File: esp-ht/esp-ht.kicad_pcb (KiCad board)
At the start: 2 copper layers, 25.4 x 54.6 mm, 28 parts, among them P1 CONN_01X02, P2 CONN_01X02, SW1 SW_PUSH_SMALL, SW2 SW_PUSH_SMALL, U1 ESP-12E, U2 MCP1700-3.0, U3 SI7021

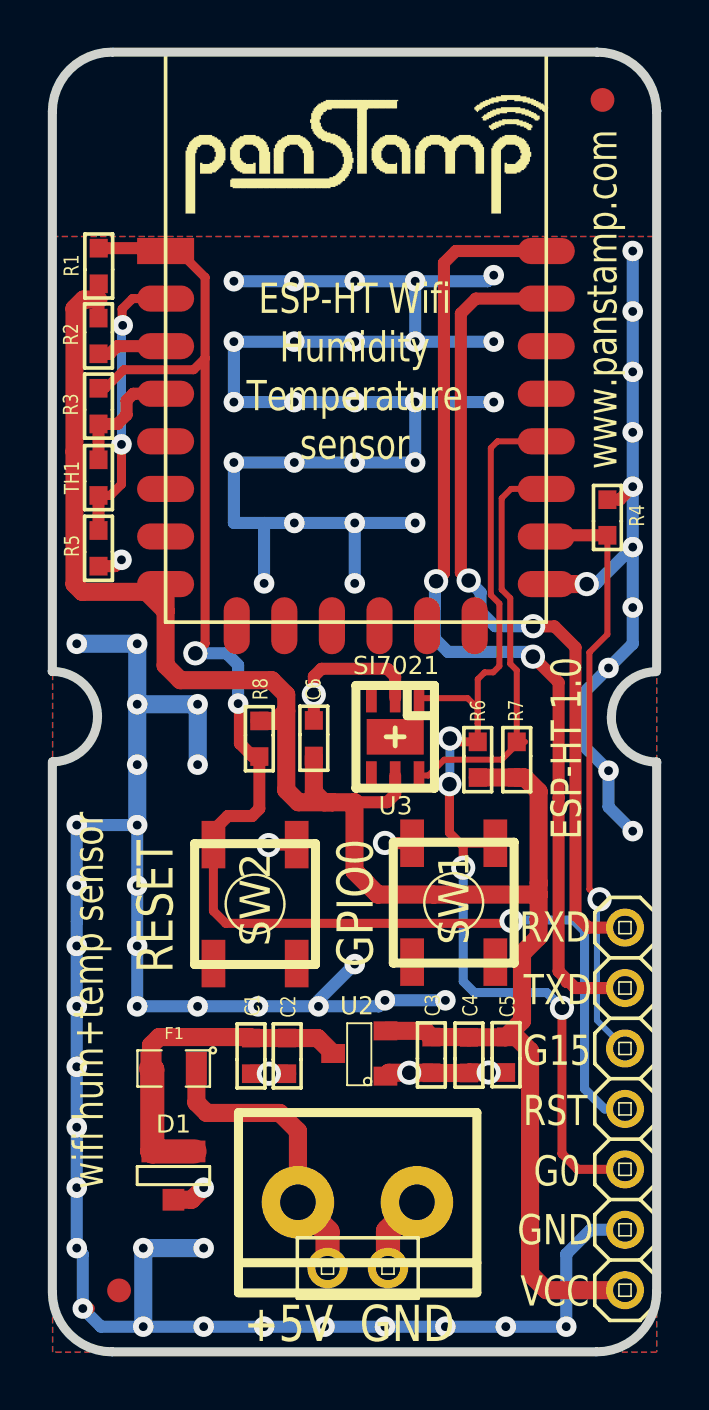
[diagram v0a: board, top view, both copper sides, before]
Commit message: BMP180 pressure sensor added to the circuit
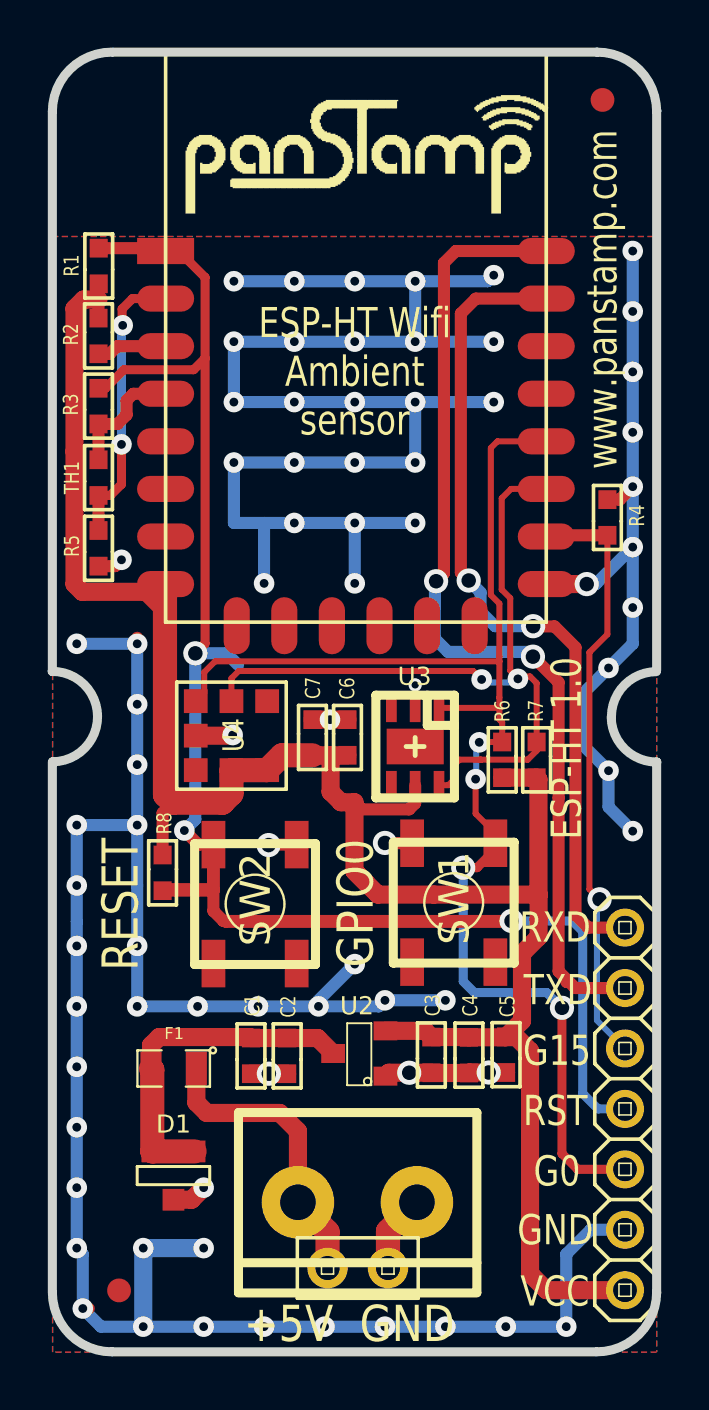
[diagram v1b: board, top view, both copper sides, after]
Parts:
- added C7: 1u, mysmd:SM0603S, F.Cu at (146.8, 73.8)
- added U4: BMP180, mysmd:BMP180, F.Cu at (143.4, 73.7)
- moved R8 6.95 mm to (140.5, 79.5)
- moved C6 1.42 mm to (148.3, 73.8)
- moved R6 1.03 mm to (154.8, 74.7)
- moved U3 0.93 mm to (151.1, 74.2)
- moved R7 0.84 mm to (156.2, 74.7)
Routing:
- net /RESET: track 65.2 -> 88.0 mm
- net /GPIO2: track 17.6 -> 32.2 mm, vias 0 -> 2
- net /GPIO0: track 45.6 -> 57.5 mm
- net GND: track 146.9 -> 139.8 mm, vias 54 -> 53
- net VCC: track 93.5 -> 98.2 mm
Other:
- rule via_min_drill: 0.3683 -> 0.3048
- rule via_min_size: 0.8636 -> 0.5588
- board text added: "ESP-HT Wifi Ambient sensor"
- board text removed: "ESP-HT Wifi Humidity Temperature sensor"
- board text removed: "wifi hum+temp sensor"

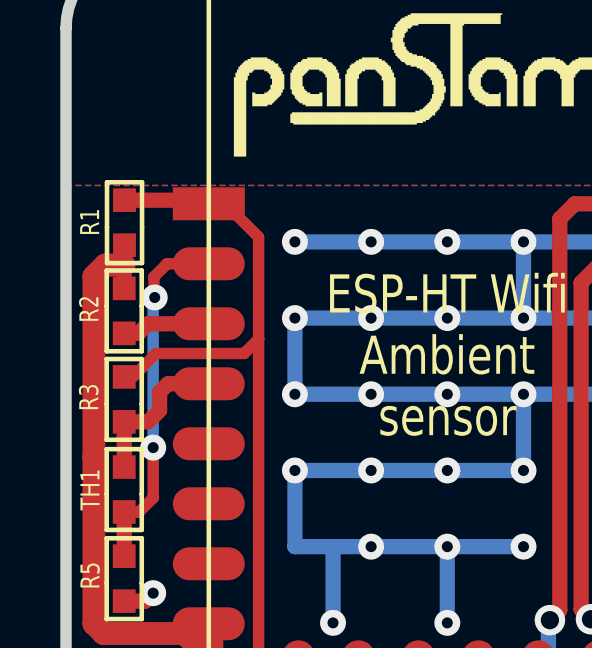
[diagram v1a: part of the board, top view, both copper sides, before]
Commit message: repeated Pull-up resistor (R1)  to RESET removed
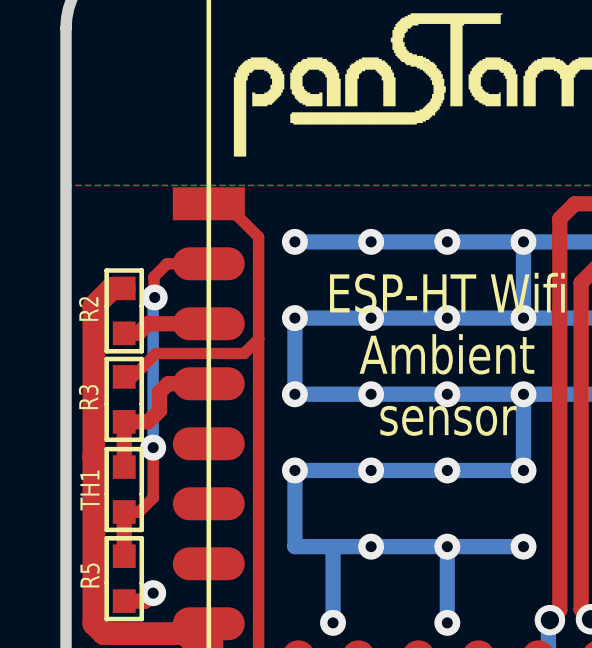
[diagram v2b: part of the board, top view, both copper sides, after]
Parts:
- removed R1: 10k, mysmd:SM0603S
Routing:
- net /RESET: track 88.0 -> 85.4 mm
- net VCC: track 98.2 -> 95.9 mm
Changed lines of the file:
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@@
-(kicad_pcb (version 4) (host pcbnew 0.201511131146+6311~30~ubuntu14.04.1-product)
+(kicad_pcb (version 4) (host pcbnew 0.201512211246+6391~39~ubuntu14.04.1-stable)
   (general
-    (links 62)
+    (links 60)
     (no_connects 0)
-    (area 135.679499 44.789499 161.480501 99.800501)
+    (area 133.447065 41.2496 163.844514 102.9716)
     (thickness 1.6002)
     (drawings 28)
-    (tracks 464)
+    (tracks 460)
     (zones 0)
-    (modules 30)
+    (modules 29)
     (nets 25)
   )
@@
   )
   (setup
-    (last_trace_width 1.016)
+    (last_trace_width 0.762)
     (user_trace_width 0.254)
     (user_trace_width 0.381)
@@
   )
   (module mysmd:SM0603S (layer Front)
-    (at 137.83 53.97 270)
-    (attr smd)
-    (fp_text reference R1 (at -0.02 1.14 270) (layer F.SilkS)
-      (effects (font (size 0.635 0.508) (thickness 0.127)))
-    )
-    (fp_text value 10k (at 0.0762 -0.0254 270) (layer F.SilkS) hide
-      (effects (font (size 0.635 0.508) (thickness 0.127)))
-    )
-    (fp_line (start 0.1524 -0.5842) (end -1.3462 -0.5842) (layer F.SilkS) (width 0.1524))
-    (fp_line (start -1.3462 -0.5842) (end -1.3462 0.5842) (layer F.SilkS) (width 0.1524))
-    (fp_line (start -1.3462 0.5842) (end 0.1524 0.5842) (layer F.SilkS) (width 0.1524))
-    (fp_line (start 0.1524 -0.5842) (end 1.3462 -0.5842) (layer F.SilkS) (width 0.1524))
-    (fp_line (start 1.3462 -0.5842) (end 1.3462 0.5842) (layer F.SilkS) (width 0.1524))
-    (fp_line (start 1.3462 0.5842) (end 0.1524 0.5842) (layer F.SilkS) (width 0.1524))
-    (pad 2 smd rect (at 0.7493 0 270) (size 0.7874 0.762) (layers Front F.Paste F.Mask)
-      (net 11 VCC))
-    (pad 1 smd rect (at -0.7493 0 270) (size 0.7874 0.762) (layers Front F.Paste F.Mask)
-      (net 1 /RESET))
-    (model smd/chip_cms.wrl
-      (at (xyz 0 0 0))
-      (scale (xyz 0.17 0.16 0.16))
-      (rotate (xyz 0 0 0))
-    )
-  )
-  (module mysmd:SM0603S (layer Front)
     (at 137.82 56.91 90)
     (attr smd)
@@
   (segment (start 142.3 54.45) (end 141.19 53.34) (width 0.381) (layer Front) (net 1))
   (segment (start 141.19 53.34) (end 140.64 53.34) (width 0.381) (layer Front) (net 1))
-  (segment (start 137.83 53.2207) (end 140.5207 53.2207) (width 0.508) (layer Front) (net 1))
   (segment (start 140.5207 53.2207) (end 140.64 53.34) (width 0.508) (layer Front) (net 1))
   (via (at 155.18 81.5) (size 1.016) (drill 0.6096) (layers Front Back) (net 1))
@@
   (segment (start 159.21 65.2893) (end 156.6907 65.2893) (width 0.508) (layer Front) (net 10))
   (segment (start 156.6907 65.2893) (end 156.64 65.34) (width 0.508) (layer Front) (net 10))
+  (segment (start 137.82 56.1607) (end 137.4127 56.1607) (width 0.762) (layer Front) (net 11))
+  (segment (start 137.4127 56.1607) (end 136.81 56.7634) (width 0.762) (layer Front) (net 11))
   (segment (start 151.13 75.793) (end 151.13 76.5556) (width 0.508) (layer Front) (net 11))
   (segment (start 148.8796 76.8096) (end 148.58 76.51) (width 0.508) (layer Front) (net 11))
@@
   (segment (start 156.3116 75.5523) (end 156.2354 75.4761) (width 0.762) (layer Front) (net 11))
   (segment (start 136.81 61.77) (end 136.81 67.341) (width 0.762) (layer Front) (net 11))
-  (segment (start 137.19 55.38) (end 136.81 55.76) (width 0.762) (layer Front) (net 11))
-  (segment (start 136.81 55.76) (end 136.81 61.77) (width 0.762) (layer Front) (net 11))
-  (segment (start 137.82 55.38) (end 137.19 55.38) (width 0.762) (layer Front) (net 11))
+  (segment (start 136.81 56.7634) (end 136.81 61.77) (width 0.762) (layer Front) (net 11))
   (segment (start 137.1346 67.6656) (end 139.827 67.6656) (width 0.762) (layer Front) (net 11))
   (segment (start 136.81 67.341) (end 137.1346 67.6656) (width 0.762) (layer Front) (net 11))
@@
   (segment (start 149.07 79.9) (end 148.58 79.41) (width 0.508) (layer Front) (net 11))
   (segment (start 156.32 81.43) (end 156.32 80.39) (width 0.762) (layer Front) (net 11))
-  (segment (start 137.82 56.1607) (end 137.82 55.38) (width 0.508) (layer Front) (net 11))
-  (segment (start 137.82 55.38) (end 137.82 54.7293) (width 0.508) (layer Front) (net 11))
-  (segment (start 137.82 54.7293) (end 137.83 54.7193) (width 0.508) (layer Front) (net 11))
   (segment (start 149.87982 86.1175) (end 151.5468 86.1175) (width 0.762) (layer Front) (net 11))
   (segment (start 151.5468 86.1175) (end 151.81 86.3807) (width 0.762) (layer Front) (net 11))

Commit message: Version changed
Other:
- rule pad_to_mask_clearance: 0.254 -> 0.0762
- board text added: "v.1.0"
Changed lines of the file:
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@@
-(kicad_pcb (version 4) (host pcbnew 0.201512211246+6391~39~ubuntu14.04.1-stable)
+(kicad_pcb (version 4) (host pcbnew 0.201601211448+6504~42~ubuntu14.04.1-product)
   (general
     (links 60)
@@
     (area 133.447065 41.2496 163.844514 102.9716)
     (thickness 1.6002)
-    (drawings 28)
+    (drawings 29)
     (tracks 460)
     (zones 0)
@@
   )
   (setup
-    (last_trace_width 0.762)
+    (last_trace_width 0.1524)
     (user_trace_width 0.254)
     (user_trace_width 0.381)
@@
     (pad_size 1.7 1.7)
     (pad_drill 1.016)
-    (pad_to_mask_clearance 0.254)
+    (pad_to_mask_clearance 0.0762)
+    (solder_mask_min_width 0.1016)
     (aux_axis_origin 0 0)
     (visible_elements FFFFF7FF)
     (pcbplotparams
-      (layerselection 0x010e0_80000001)
+      (layerselection 0x010e0_ffffffff)
       (usegerberextensions true)
       (excludeedgelayer true)
@@
       (net 4 GND))
   )
+  (gr_text v.1.0 (at 140.208 95.25) (layer F.SilkS)
+    (effects (font (size 1.524 1.27) (thickness 0.1778)))
+  )
   (gr_text "ESP-HT Wifi\nAmbient\nsensor" (at 148.59 58.42) (layer F.SilkS)
     (effects (font (size 1.27 1.016) (thickness 0.1524)))
@@
     (effects (font (size 1.524 1.27) (thickness 0.1778)))
   )
-  (gr_text RESET (at 138.7602 80.7974 90) (layer F.SilkS)
+  (gr_text RESET (at 138.684 80.772 90) (layer F.SilkS)
     (effects (font (size 1.524 1.27) (thickness 0.1778)))
   )

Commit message: Minor changes
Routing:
- net /RESET: track 85.4 -> 83.4 mm
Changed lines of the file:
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@@
-(kicad_pcb (version 4) (host pcbnew 0.201601211448+6504~42~ubuntu14.04.1-product)
+(kicad_pcb (version 4) (host pcbnew 0.201601262101+6516~42~ubuntu14.04.1-product)
   (general
     (links 60)
@@
     (thickness 1.6002)
     (drawings 29)
-    (tracks 460)
+    (tracks 458)
     (zones 0)
     (modules 29)
@@
     (mod_text_size 1.524 1.524)
     (mod_text_width 0.3048)
-    (pad_size 1.7 1.7)
-    (pad_drill 1.016)
+    (pad_size 1.6 1.6)
+    (pad_drill 1)
     (pad_to_mask_clearance 0.0762)
     (solder_mask_min_width 0.1016)
@@
     (fp_line (start 1.016 -0.254) (end 1.524 -0.254) (layer F.SilkS) (width 0.06604))
     (fp_line (start 1.016 0.254) (end 1.016 -0.254) (layer F.SilkS) (width 0.06604))
-    (pad 1 thru_hole circle (at -1.27 0) (size 1.7 1.7) (drill 1.016) (layers *.Cu F.Paste F.SilkS F.Mask)
+    (pad 1 thru_hole circle (at -1.27 0) (size 1.7 1.7) (drill 1.016) (layers *.Cu *.Mask F.Paste F.SilkS)
       (net 24 "Net-(F1-Pad1)"))
-    (pad 2 thru_hole circle (at 1.27 0) (size 1.7 1.7) (drill 1.016) (layers *.Cu F.Paste F.SilkS F.Mask)
+    (pad 2 thru_hole circle (at 1.27 0) (size 1.7 1.7) (drill 1.016) (layers *.Cu *.Mask F.Paste F.SilkS)
       (net 4 GND))
   )
@@
     (fp_line (start 6.35 0.635) (end 6.985 1.27) (layer F.SilkS) (width 0.1524))
     (fp_line (start 8.255 1.27) (end 6.985 1.27) (layer F.SilkS) (width 0.1524))
-    (pad 1 thru_hole circle (at -7.62 0 270) (size 1.6 1.6) (drill 1) (layers *.Cu F.Paste F.SilkS F.Mask)
+    (pad 1 thru_hole circle (at -7.62 0 270) (size 1.6 1.6) (drill 1) (layers *.Cu *.Mask F.Paste F.SilkS)
       (net 2 /RXD))
-    (pad 2 thru_hole circle (at -5.08 0 270) (size 1.6 1.6) (drill 1) (layers *.Cu F.Paste F.SilkS F.Mask)
+    (pad 2 thru_hole circle (at -5.08 0 270) (size 1.6 1.6) (drill 1) (layers *.Cu *.Mask F.Paste F.SilkS)
       (net 3 /TXD))
-    (pad 3 thru_hole circle (at -2.54 0 270) (size 1.6 1.6) (drill 1) (layers *.Cu F.Paste F.SilkS F.Mask)
+    (pad 3 thru_hole circle (at -2.54 0 270) (size 1.6 1.6) (drill 1) (layers *.Cu *.Mask F.Paste F.SilkS)
       (net 10 /GPIO15))
-    (pad 4 thru_hole circle (at 0 0 270) (size 1.6 1.6) (drill 1) (layers *.Cu F.Paste F.SilkS F.Mask)
+    (pad 4 thru_hole circle (at 0 0 270) (size 1.6 1.6) (drill 1) (layers *.Cu *.Mask F.Paste F.SilkS)
       (net 1 /RESET))
-    (pad 5 thru_hole circle (at 2.54 0 270) (size 1.6 1.6) (drill 1) (layers *.Cu F.Paste F.SilkS F.Mask)
+    (pad 5 thru_hole circle (at 2.54 0 270) (size 1.6 1.6) (drill 1) (layers *.Cu *.Mask F.Paste F.SilkS)
       (net 5 /GPIO0))
-    (pad 6 thru_hole circle (at 5.08 0 270) (size 1.6 1.6) (drill 1) (layers *.Cu F.Paste F.SilkS F.Mask)
+    (pad 6 thru_hole circle (at 5.08 0 270) (size 1.6 1.6) (drill 1) (layers *.Cu *.Mask F.Paste F.SilkS)
       (net 4 GND))
-    (pad 7 thru_hole circle (at 7.62 0 270) (size 1.6 1.6) (drill 1) (layers *.Cu F.Paste F.SilkS F.Mask)
+    (pad 7 thru_hole circle (at 7.62 0 270) (size 1.6 1.6) (drill 1) (layers *.Cu *.Mask F.Paste F.SilkS)
       (net 11 VCC))
   )
@@
   (segment (start 142.64994 78.29064) (end 142.64994 80.1624) (width 0.508) (layer Front) (net 1))
   (segment (start 142.64994 80.1624) (end 142.64994 80.2259) (width 0.508) (layer Front) (net 1))
-  (segment (start 143.1988 70.25) (end 141.89 70.25) (width 0.508) (layer Back) (net 1))
   (via (at 141.89 70.25) (size 1.016) (drill 0.6096) (layers Front Back) (net 1))
-  (segment (start 143.6878 70.739) (end 143.1988 70.25) (width 0.508) (layer Back) (net 1))
   (segment (start 140.5128 80.2259) (end 142.64994 80.2259) (width 0.508) (layer Front) (net 1))
   (segment (start 142.5194 80.2386) (end 142.64994 80.2386) (width 0.508) (layer Front) (net 1))
